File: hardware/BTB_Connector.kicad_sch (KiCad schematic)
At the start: 1 part, among them J4 5024268012

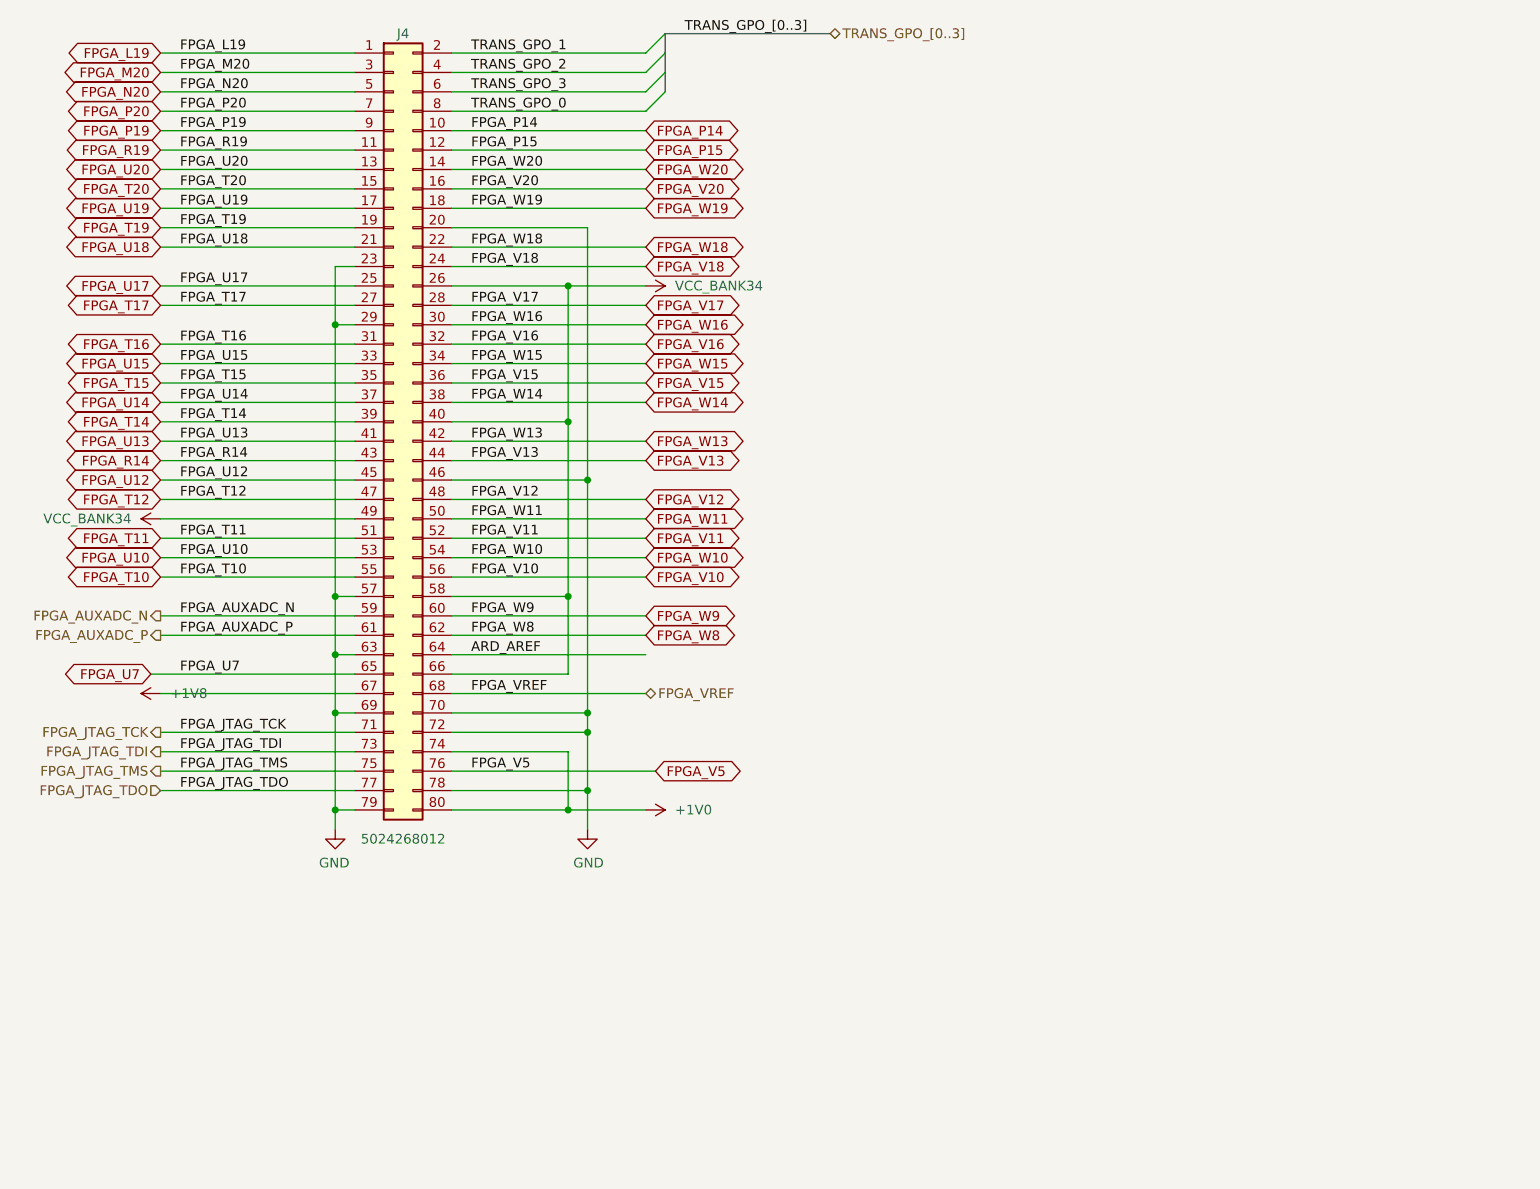
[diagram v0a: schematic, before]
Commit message: add sdio level shift ciruit
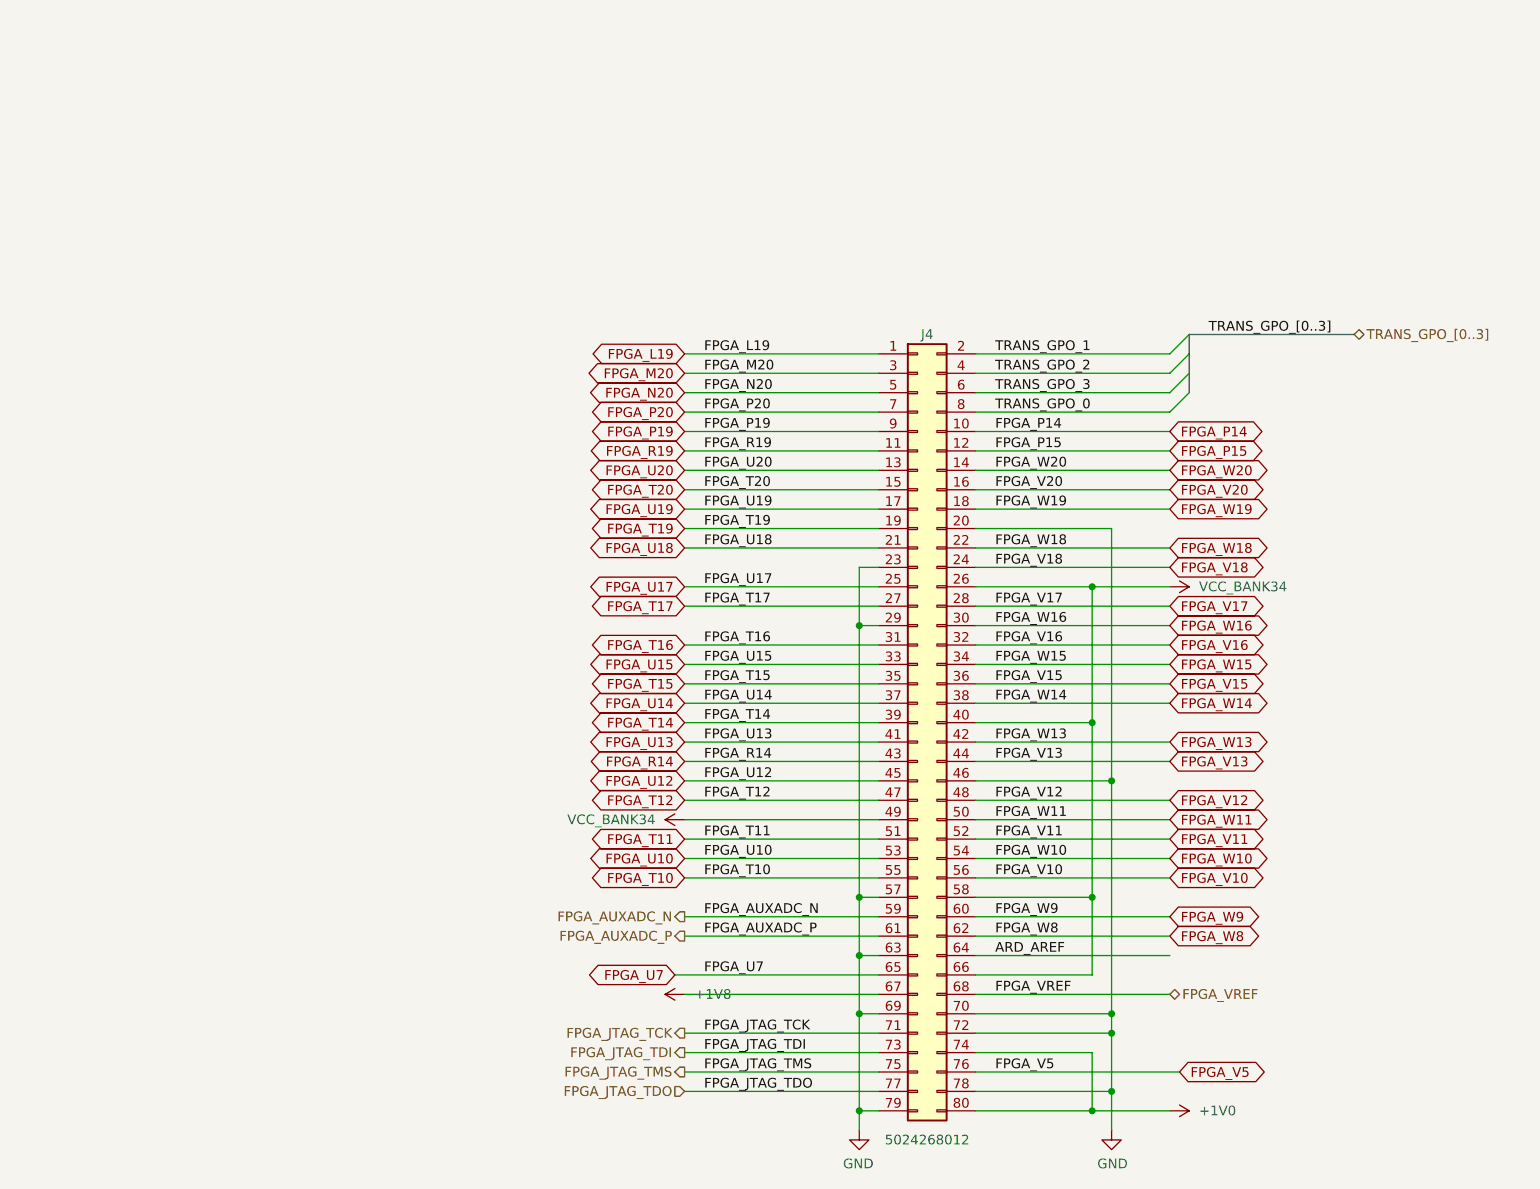
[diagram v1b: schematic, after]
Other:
- moved on the sheet: J4
